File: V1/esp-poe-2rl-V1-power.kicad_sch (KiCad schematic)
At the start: 32 parts, among them U1 TPS2376DDAR-H, U2 TX4138, U3 SY8089A1AAC

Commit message: Added temperature sensor
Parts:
- U2: footprint Tales:SOIC-8-1EP_3.9x4.9mm_P1.27mm_EP2.29x3mm_ThermalVias -> Tales:SOIC-8-1EP_3.9x4.9mm_P1.27mm_EP2.41x3.81mm_ThermalVias

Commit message: Reviewing board for fabrication
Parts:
- U3: footprint Tales:TSOT-23-5 -> Tales:SOT-23-5_Shorter_Pins
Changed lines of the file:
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@@
 			)
 		)
-		(property "Footprint" "Tales:TSOT-23-5"
+		(property "Footprint" "Tales:SOT-23-5_Shorter_Pins"
 			(at 80.01 152.4 0)
 			(effects

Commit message: Selecting components at JLCPCB
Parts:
- D1: LCSC Part # C115922 -> C132936; Mfr Brightking -> STMicroelectronics; Mfr PN SMAJ58A/TR13 -> SMAJ58A-TR; Vendor PN C115922 -> C132936
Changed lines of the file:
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@@
 			)
 		)
-		(property "LCSC Part #" "C115922"
+		(property "LCSC Part #" "C132936"
 			(at 30.48 45.085 90)
 			(effects
@@
 			)
 		)
-		(property "Mfr" "Brightking"
+		(property "Mfr" "STMicroelectronics"
 			(at 27.94 40.64 0)
 			(effects
@@
 			)
 		)
-		(property "Mfr PN" "SMAJ58A/TR13"
+		(property "Mfr PN" "SMAJ58A-TR"
 			(at 27.94 40.64 0)
 			(effects
@@
 			)
 		)
-		(property "Vendor PN" "C115922"
+		(property "Vendor PN" "C132936"
 			(at 30.48 45.085 90)
 			(effects

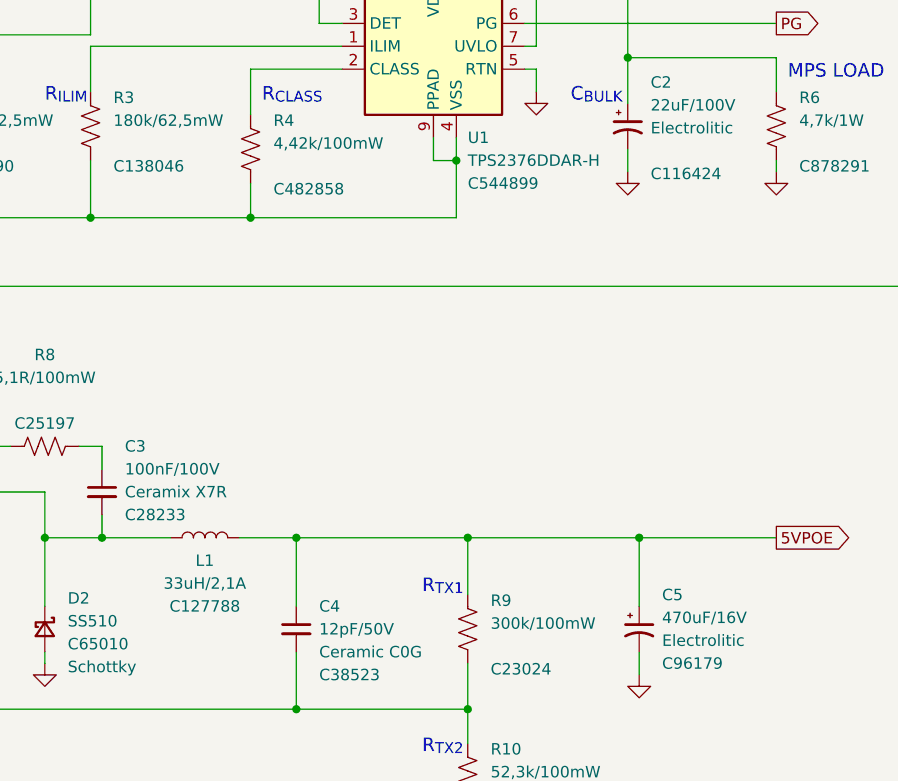
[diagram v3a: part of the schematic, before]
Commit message: Replaced RJ45 connector
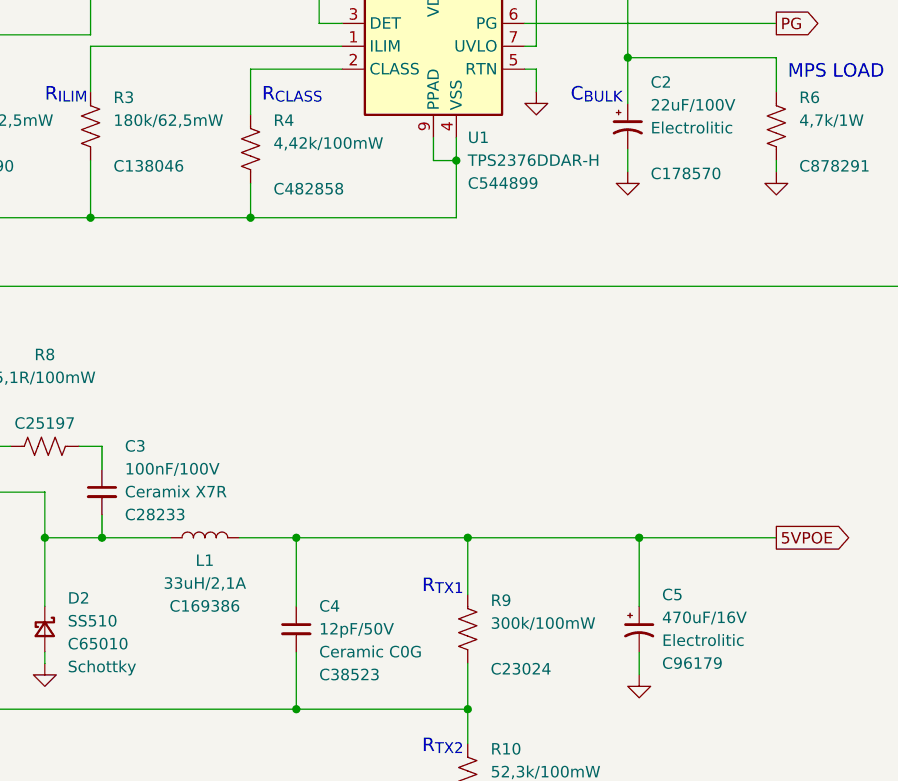
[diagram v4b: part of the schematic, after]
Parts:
- C2: LCSC Part # C116424 -> C178570; Mfr Semtech -> Panasonic; Mfr PN CS2A220M-CRF10 -> EEEFK2A220P; Vendor PN C116424 -> C178570
- L1: LCSC Part # C127788 -> C169386; Mfr PN SWRH1205B-330MT -> SWRB1205S-330MT; Vendor PN C127788 -> C169386
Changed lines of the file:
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@@
 			)
 		)
-		(property "LCSC Part #" "C127788"
+		(property "LCSC Part #" "C169386"
 			(at 95.25 104.14 90)
 			(effects
@@
 			)
 		)
-		(property "Mfr PN" "SWRH1205B-330MT"
+		(property "Mfr PN" "SWRB1205S-330MT"
 			(at 95.25 96.52 0)
 			(effects
@@
 			)
 		)
-		(property "Vendor PN" "C127788"
+		(property "Vendor PN" "C169386"
 			(at 95.25 96.52 0)
 			(effects
@@
 			)
 		)
-		(property "LCSC Part #" "C116424"
+		(property "LCSC Part #" "C178570"
 			(at 144.78 56.0832 0)
 			(effects
@@
 			)
 		)
-		(property "Mfr" "Semtech"
+		(property "Mfr" "Panasonic"
 			(at 142.24 50.8 0)
 			(effects
@@
 			)
 		)
-		(property "Mfr PN" "CS2A220M-CRF10"
+		(property "Mfr PN" "EEEFK2A220P"
 			(at 142.24 50.8 0)
 			(effects
@@
 			)
 		)
-		(property "Vendor PN" "C116424"
+		(property "Vendor PN" "C178570"
 			(at 142.24 50.8 0)
 			(effects

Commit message: Prefab checks
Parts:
- D5: value GREEN -> EMERALD; LCSC Part # C72043 -> C2984266; Mfr Everlight -> Everlight eLEC; Mfr PN 19-217/GHC-YR1S2/3T -> 19-213/GHC-XS1T1/5T; Vendor PN C72043 -> C2984266
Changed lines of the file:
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@@
 			)
 		)
-		(property "Value" "GREEN"
+		(property "Value" "EMERALD"
 			(at 46.99 181.61 90)
 			(effects
@@
 			)
 		)
-		(property "Mfr" "Everlight"
+		(property "Mfr" "Everlight eLEC"
 			(at 44.45 180.34 0)
 			(effects
@@
 			)
 		)
-		(property "Mfr PN" "19-217/GHC-YR1S2/3T"
+		(property "Mfr PN" "19-213/GHC-XS1T1/5T"
 			(at 44.45 180.34 0)
 			(effects
@@
 			)
 		)
-		(property "Vendor PN" "C72043"
+		(property "Vendor PN" "C2984266"
 			(at 44.45 180.34 0)
 			(effects
@@
 			)
 		)
-		(property "LCSC Part #" "C72043"
+		(property "LCSC Part #" "C2984266"
 			(at 46.99 186.69 90)
 			(effects

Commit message: Files for release 1.3.0
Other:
- title: (none) -> ESP 2x Relay Output Module with PoE
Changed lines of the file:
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@@
 	(generator_version "8.0")
 	(paper "A4")
+	(title_block
+		(title "ESP 2x Relay Output Module with PoE")
+		(date "2025-06-29")
+		(rev "V1.3")
+	)
 	(junction
 		(at 142.24 21.59)

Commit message: Fabrication updates
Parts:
- D5: value EMERALD -> WHITE; LCSC Part # C2984266 -> C2290; Mfr Everlight eLEC -> Hubei KENTO Elec; Mfr PN 19-213/GHC-XS1T1/5T -> KT-0603W; Package 0603 -> 0603/1608; Vendor PN C2984266 -> C2290
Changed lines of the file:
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@@
 			)
 		)
-		(property "Value" "EMERALD"
+		(property "Value" "WHITE"
 			(at 46.99 181.61 90)
 			(effects
@@
 			)
 		)
-		(property "Mfr" "Everlight eLEC"
+		(property "Mfr" "Hubei KENTO Elec"
 			(at 44.45 180.34 0)
 			(effects
@@
 			)
 		)
-		(property "Mfr PN" "19-213/GHC-XS1T1/5T"
+		(property "Mfr PN" "KT-0603W"
 			(at 44.45 180.34 0)
 			(effects
@@
 			)
 		)
-		(property "Vendor PN" "C2984266"
+		(property "Vendor PN" "C2290"
 			(at 44.45 180.34 0)
 			(effects
@@
 			)
 		)
-		(property "LCSC Part #" "C2984266"
+		(property "LCSC Part #" "C2290"
 			(at 46.99 186.69 90)
 			(effects
@@
 			)
 		)
-		(property "Package" "0603"
+		(property "Package" "0603/1608"
 			(at 44.45 180.34 0)
 			(effects
